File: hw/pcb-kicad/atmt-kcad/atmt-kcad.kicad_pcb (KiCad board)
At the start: 2 copper layers, 56 x 62.5 mm, 38 parts, among them J1 Reset, J10 JTAG, J11 BAT+, J12 BAT-, J13 Steering, J14 Motor, J15 BOOT, J16 Light, J17 Buck/Boost, J2 PowerSw, J3 US-Front, J4 US-Rear, J5 US-Right, J6 US-Left, J7 I2Cx2, J8 PRG, J9 I2C_1, U1 ESP32-WROOM-32U, U2 LP2988-3.3_SOIC8_VSSOP8, U3 4504, U4 L293DD

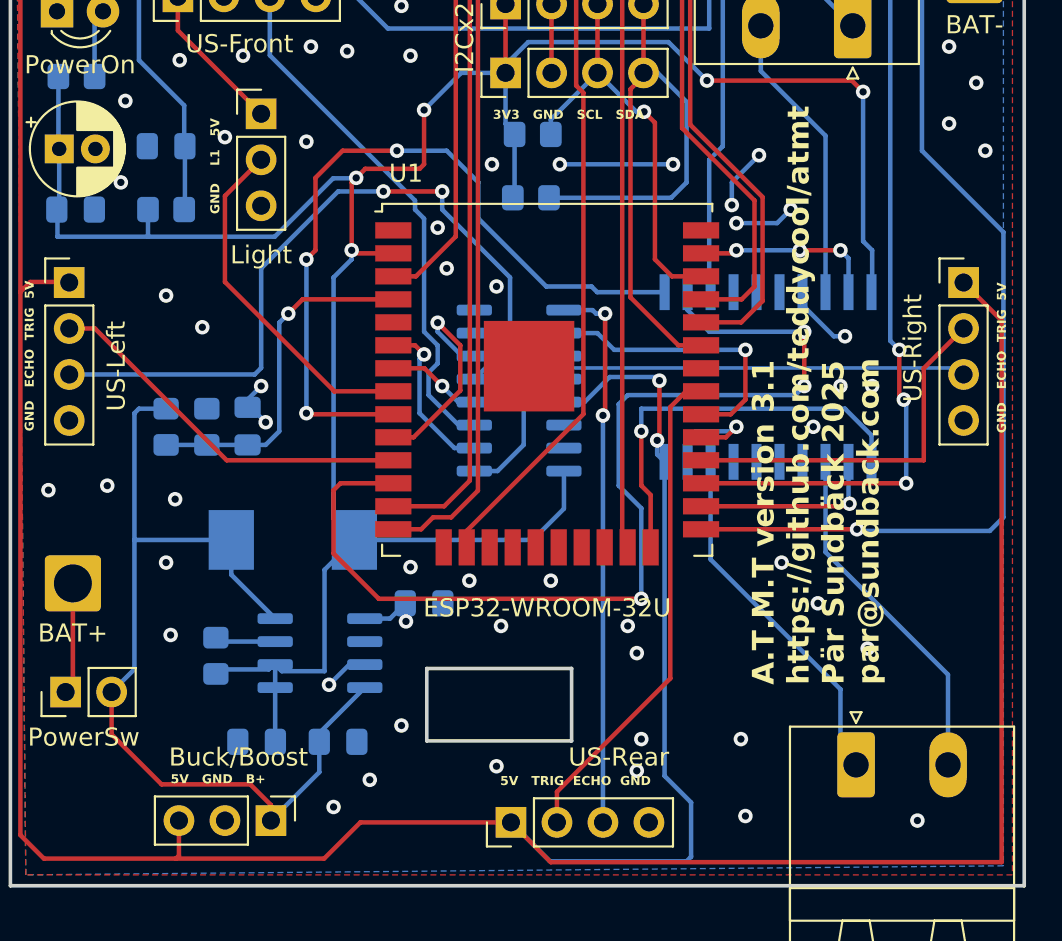
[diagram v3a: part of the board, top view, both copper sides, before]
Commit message: New PCB version, HW 3.2
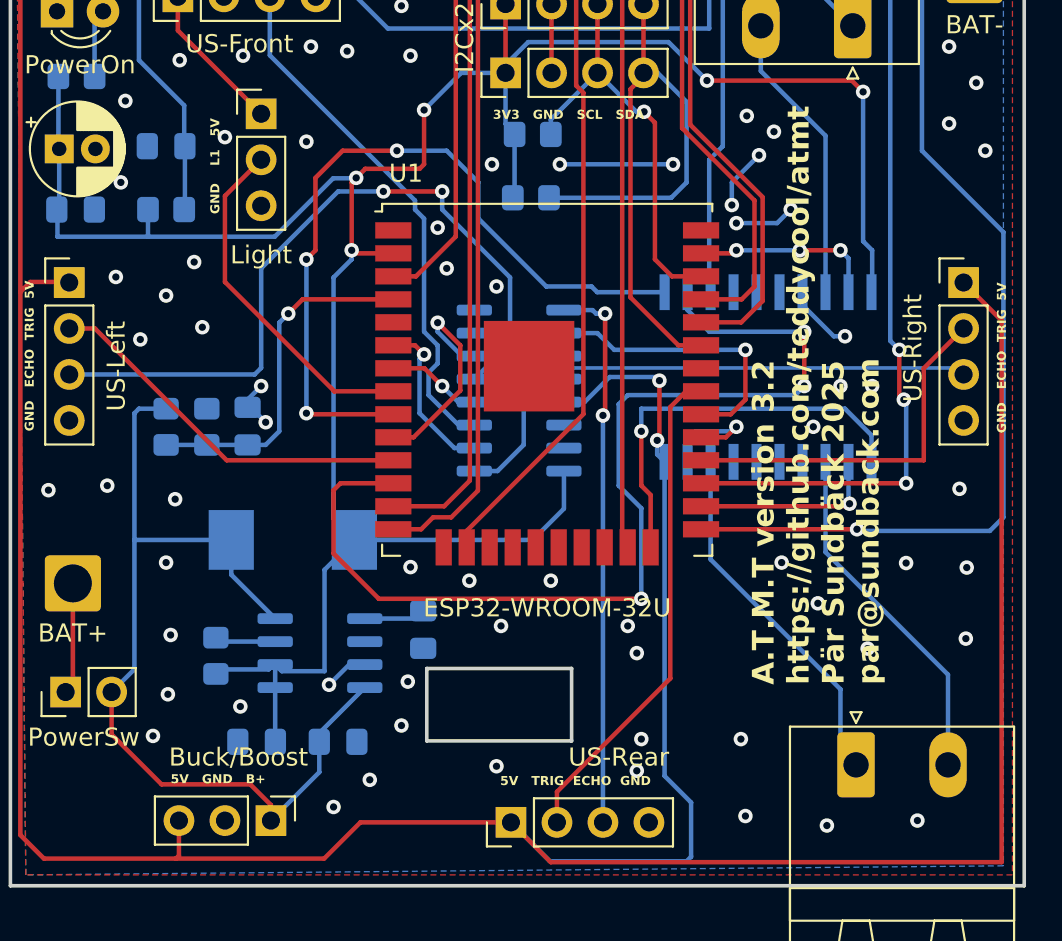
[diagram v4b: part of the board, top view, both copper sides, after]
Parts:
- moved C8 1.45 mm to (115.0, 109.0), turned to -90 degrees
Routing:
- net Net-(U2-BP): track 2.59 -> 3.40 mm
- net GND: vias 68 -> 81
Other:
- board text added: "A.T.M.T version 3.2 https://github.com/teddycool/atmt Pär Sundbäck 2025 par@sundback.com"
- board text removed: "A.T.M.T version 3.1 https://github.com/teddycool/atmt Pär Sundbäck 2025 par@sundback.com"
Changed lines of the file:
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@@
 	(footprint "Capacitor_SMD:C_0805_2012Metric_Pad1.18x1.45mm_HandSolder"
 		(layer "B.Cu")
-		(at 115 107.5)
+		(at 114.95 108.95 -90)
 		(descr "Capacitor SMD 0805 (2012 Metric), square (rectangular) end terminal, IPC_7351 nominal with elongated pad for handsoldering. (Body size source: IPC-SM-782 page 76, https://www.pcb-3d.com/wordpress/wp-content/uploads/ipc-sm-782a_amendment_1_and_2.pdf, https://docs.google.com/spreadsheets/d/1BsfQQcO9C6DZCsRaXUlFlo91Tg2WpOkGARC1WS5S8t0/edit?usp=sharing), generated with kicad-footprint-generator")
 		(tags "capacitor handsolder")
 		(property "Reference" "C8"
-			(at 0 1.68 0)
+			(at 0.2 -1.8 90)
 			(layer "B.SilkS")
 			(effects
@@
 		)
 		(property "Value" "100n"
-			(at 0 -1.68 0)
+			(at 0 -1.68 90)
 			(layer "B.Fab")
 			(effects
@@
 		)
 		(property "Footprint" "Capacitor_SMD:C_0805_2012Metric_Pad1.18x1.45mm_HandSolder"
-			(at 0 0 180)
+			(at 0 0 90)
 			(unlocked yes)
 			(layer "B.Fab")
@@
 		)
 		(property "Datasheet" ""
-			(at 0 0 180)
+			(at 0 0 90)
 			(unlocked yes)
 			(layer "B.Fab")
@@
 		)
 		(property "Description" ""
-			(at 0 0 180)
+			(at 0 0 90)
 			(unlocked yes)
 			(layer "B.Fab")
@@
 		(attr smd)
 		(fp_line
-			(start 0.261252 -0.735)
-			(end -0.261252 -0.735)
+			(start 0.261252 0.735)
+			(end -0.261252 0.735)
 			(stroke
 				(width 0.12)
@@
 		)
 		(fp_line
-			(start 0.261252 0.735)
-			(end -0.261252 0.735)
+			(start 0.261252 -0.735)
+			(end -0.261252 -0.735)
 			(stroke
 				(width 0.12)
@@
 		)
 		(fp_line
-			(start -1.88 -0.98)
-			(end 1.88 -0.98)
+			(start -1.88 0.98)
+			(end -1.88 -0.98)
 			(stroke
 				(width 0.05)
@@
 		)
 		(fp_line
-			(start -1.88 0.98)
-			(end -1.88 -0.98)
+			(start 1.88 0.98)
+			(end -1.88 0.98)
 			(stroke
 				(width 0.05)
@@
 		)
 		(fp_line
-			(start 1.88 -0.98)
-			(end 1.88 0.98)
+			(start -1.88 -0.98)
+			(end 1.88 -0.98)
 			(stroke
 				(width 0.05)
@@
 		)
 		(fp_line
-			(start 1.88 0.98)
-			(end -1.88 0.98)
+			(start 1.88 -0.98)
+			(end 1.88 0.98)
 			(stroke
 				(width 0.05)
@@
 		)
 		(fp_line
-			(start -1 -0.625)
-			(end 1 -0.625)
+			(start -1 0.625)
+			(end -1 -0.625)
 			(stroke
 				(width 0.1)
@@
 		)
 		(fp_line
-			(start -1 0.625)
-			(end -1 -0.625)
+			(start 1 0.625)
+			(end -1 0.625)
 			(stroke
 				(width 0.1)
@@
 		)
 		(fp_line
-			(start 1 -0.625)
-			(end 1 0.625)
+			(start -1 -0.625)
+			(end 1 -0.625)
 			(stroke
 				(width 0.1)
@@
 		)
 		(fp_line
-			(start 1 0.625)
-			(end -1 0.625)
+			(start 1 -0.625)
+			(end 1 0.625)
 			(stroke
 				(width 0.1)
@@
 		)
 		(fp_text user "${REFERENCE}"
-			(at 0 0 0)
+			(at 0 0 90)
 			(layer "B.Fab")
 			(effects
@@
 		)
 		(pad "1" smd roundrect
-			(at -1.0375 0)
+			(at -1.0375 0 270)
 			(size 1.175 1.45)
 			(layers "B.Cu" "B.Paste" "B.Mask")
@@
 		)
 		(pad "2" smd roundrect
-			(at 1.0375 0)
+			(at 1.0375 0 270)
 			(size 1.175 1.45)
 			(layers "B.Cu" "B.Paste" "B.Mask")
@@
 		(tags "SOIC SO")
 		(property "Reference" "U2"
-			(at -5.25 1.75 0)
+			(at 1.525 3.9 0)
 			(layer "B.SilkS")
 			(effects
@@
 		(layer "Edge.Cuts")
 	)
+	(gr_text "A.T.M.T version 3.2\nhttps://github.com/teddycool/atmt\nPär Sundbäck 2025\npar@sundback.com"
+		(at 145.425 108.625 0)
+		(layer "B.SilkS")
+		(effects
+			(font
+				(size 1 1)
+				(thickness 0.15)
+			)
+			(justify left bottom mirror)
+		)
+	)
 	(gr_text "3V3   GND   RX   TX"
 		(at 119 65.8 0)
@@
 		)
 	)
-	(gr_text "A.T.M.T version 3.1\nhttps://github.com/teddycool/atmt\nPär Sundbäck 2025\npar@sundback.com"
+	(gr_text "A.T.M.T version 3.2\nhttps://github.com/teddycool/atmt\nPär Sundbäck 2025\npar@sundback.com"
 		(at 140.25 112 90)
 		(layer "F.SilkS")
@@
 	)
 	(via
+		(at 141.625 105.275)
+		(size 0.8)
+		(drill 0.4)
+		(layers "F.Cu" "B.Cu")
+		(free yes)
+		(net 1)
+	)
+	(via
 		(at 146 82.5)
 		(size 0.8)
@@
 	)
 	(via
+		(at 144.925 109.45)
+		(size 0.8)
+		(drill 0.4)
+		(layers "F.Cu" "B.Cu")
+		(free yes)
+		(net 1)
+	)
+	(via
 		(at 105 77.25)
 		(size 0.8)
@@
 	)
 	(via
+		(at 100.85 112.525)
+		(size 0.8)
+		(drill 0.4)
+		(layers "F.Cu" "B.Cu")
+		(free yes)
+		(net 1)
+	)
+	(via
 		(at 109.75 112)
 		(size 0.8)
@@
 	)
 	(via
+		(at 132.825 80.575)
+		(size 0.8)
+		(drill 0.4)
+		(layers "F.Cu" "B.Cu")
+		(free yes)
+		(net 1)
+	)
+	(via
 		(at 131.5 71.25)
 		(size 0.8)
@@
 	)
 	(via
+		(at 99.325 92.925)
+		(size 0.8)
+		(drill 0.4)
+		(layers "F.Cu" "B.Cu")
+		(free yes)
+		(net 1)
+	)
+	(via
 		(at 122.5 83.25)
 		(size 0.8)
@@
 	)
 	(via
+		(at 104.85 113.2)
+		(size 0.8)
+		(drill 0.4)
+		(layers "F.Cu" "B.Cu")
+		(free yes)
+		(net 1)
+	)
+	(via
 		(at 95.75 70.75)
 		(size 0.8)
@@
 	)
 	(via
+		(at 102.3 88.65)
+		(size 0.8)
+		(drill 0.4)
+		(layers "F.Cu" "B.Cu")
+		(free yes)
+		(net 1)
+	)
+	(via
 		(at 106.25 97.5)
 		(size 0.8)
@@
 	)
 	(via
+		(at 144.975 105.525)
+		(size 0.8)
+		(drill 0.4)
+		(layers "F.Cu" "B.Cu")
+		(free yes)
+		(net 1)
+	)
+	(via
 		(at 135.25 85.75)
 		(size 0.8)
@@
 	)
 	(via
+		(at 137.25 119.775)
+		(size 0.8)
+		(drill 0.4)
+		(layers "F.Cu" "B.Cu")
+		(free yes)
+		(net 1)
+	)
+	(via
 		(at 97.75 70.75)
 		(size 0.8)
@@
 	)
 	(via
+		(at 100.025 114.825)
+		(size 0.8)
+		(drill 0.4)
+		(layers "F.Cu" "B.Cu")
+		(free yes)
+		(net 1)
+	)
+	(via
 		(at 142.25 119.5)
 		(size 0.8)
@@
 	)
 	(via
+		(at 144.575 101.175)
+		(size 0.8)
+		(drill 0.4)
+		(layers "F.Cu" "B.Cu")
+		(free yes)
+		(net 1)
+	)
+	(via
 		(at 133.5 82.75)
 		(size 0.8)
@@
 	)
 	(via
-		(at 114 108.5)
+		(at 114.1 111.825)
 		(size 0.8)
 		(drill 0.4)
@@
 	)
 	(via
+		(at 97.975 89.475)
+		(size 0.8)
+		(drill 0.4)
+		(layers "F.Cu" "B.Cu")
+		(free yes)
+		(net 1)
+	)
+	(via
 		(at 110 118.75)
 		(size 0.8)
@@
 	)
 	(via
+		(at 134.325 81.45)
+		(size 0.8)
+		(drill 0.4)
+		(layers "F.Cu" "B.Cu")
+		(free yes)
+		(net 1)
+	)
+	(via
 		(at 122 106.25)
 		(size 0.8)
@@
 	(segment
 		(start 111.725 108.345)
-		(end 113.1175 108.345)
+		(end 114.5175 108.345)
 		(width 0.25)
 		(layer "B.Cu")
@@
 	)
 	(segment
-		(start 113.1175 108.345)
-		(end 113.9625 107.5)
+		(start 114.5175 108.345)
+		(end 114.95 107.9125)
 		(width 0.25)
 		(layer "B.Cu")
